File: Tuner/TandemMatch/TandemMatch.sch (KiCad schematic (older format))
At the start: 60 parts, among them J1 Conn_01x02, J10 Conn_01x01, J11 Conn_01x01, J12 Conn_01x01, J13 Conn_01x01, J14 Conn_01x01, J15 Conn_01x01, J16 Conn_01x01, J17 Conn_01x02, J18 Conn_Coaxial, J19 Conn_01x02, J2 Conn_01x02, J20 Conn_Coaxial, J21 Conn_01x01, J22 Conn_01x01, J23 Conn_01x01, J24 Conn_01x01, J25 Conn_01x01, J26 Conn_01x01, J27 Conn_01x01, J28 Conn_01x01, J29 Conn_01x01, J3 Conn_Coaxial, J30 Conn_01x01, J31 Conn_01x01, J32 Conn_01x01, J33 Conn_01x03, J34 Conn_01x01, J35 Conn_01x01, J36 Conn_01x01, J37 Conn_01x01, J38 Conn_01x01, J39 Conn_01x01, J4 Conn_Coaxial, J40 Conn_01x01, J41 Conn_01x01, J42 Conn_01x01, J5 Conn_01x01, J6 Conn_01x01, J7 Conn_01x01, J78 Conn_01x01, J79 Conn_01x01, J8 Conn_01x01, J9 Conn_01x01

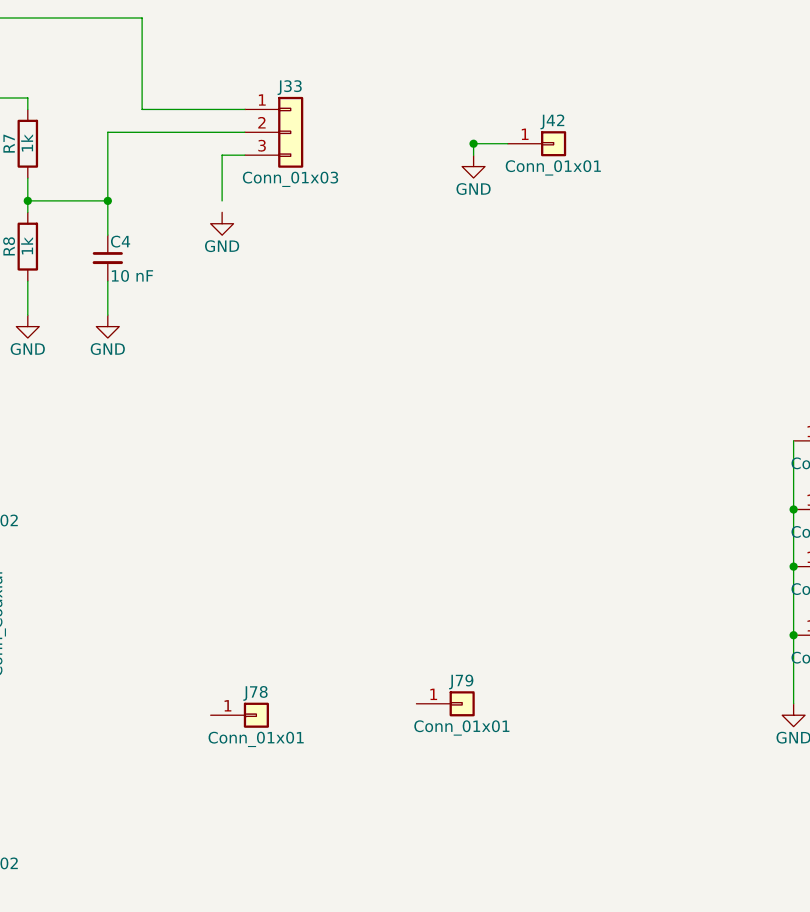
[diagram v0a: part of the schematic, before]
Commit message: Added new DelayLine board, modified TandemMatch
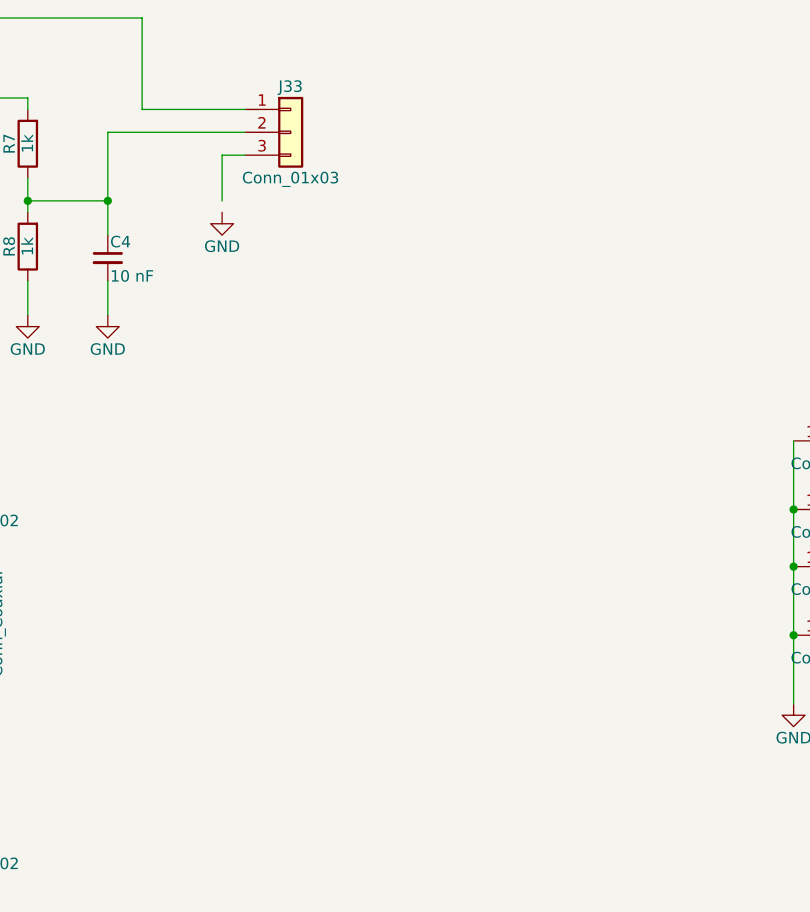
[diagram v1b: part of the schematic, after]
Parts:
- removed J42: Conn_01x01, Pin_Headers:Pin_Header_Straight_1x01_Pitch2.54mm, symbol Conn_01x01
- removed J78, J79: Conn_01x01, Connectors:1pin, symbol Conn_01x01
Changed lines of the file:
@@
 $EndComp
 $Comp
-L GND #PWR21
+L GND #PWR20
 U 1 1 5C69E6B8
 P 9450 3800
-F 0 "#PWR21" H 9450 3550 50  0001 C CNN
+F 0 "#PWR20" H 9450 3550 50  0001 C CNN
 F 1 "GND" H 9450 3650 50  0000 C CNN
 F 2 "" H 9450 3800 50  0001 C CNN
@@
 $EndComp
 $Comp
-L GND #PWR22
+L GND #PWR21
 U 1 1 5C69E7D4
 P 10250 3750
-F 0 "#PWR22" H 10250 3500 50  0001 C CNN
+F 0 "#PWR21" H 10250 3500 50  0001 C CNN
 F 1 "GND" H 10250 3600 50  0000 C CNN
 F 2 "" H 10250 3750 50  0001 C CNN
@@
 	5700 4950 5450 4950
 Connection ~ 5450 4950
-$Comp
-L Conn_01x01 J42
-U 1 1 5C6A15E5
-P 8400 1350
-F 0 "J42" H 8400 1450 50  0000 C CNN
-F 1 "Conn_01x01" H 8400 1250 50  0000 C CNN
-F 2 "Pin_Headers:Pin_Header_Straight_1x01_Pitch2.54mm" H 8400 1350 50  0001 C CNN
-F 3 "" H 8400 1350 50  0001 C CNN
-	1    8400 1350
-	1    0    0    -1
-$EndComp
-$Comp
-L GND #PWR20
-U 1 1 5C6A2A4B
-P 8050 1400
-F 0 "#PWR20" H 8050 1150 50  0001 C CNN
-F 1 "GND" H 8050 1250 50  0000 C CNN
-F 2 "" H 8050 1400 50  0001 C CNN
-F 3 "" H 8050 1400 50  0001 C CNN
-	1    8050 1400
-	1    0    0    -1
-$EndComp
-Wire Wire Line
-	8050 1350 8200 1350
-Connection ~ 8050 1350
-Wire Wire Line
-	8050 1400 8050 1350
 $Sheet
 S 9500 5450 1550 850
@@
 	5050 2550 5050 2800
 Connection ~ 5050 2800
-$Comp
-L Conn_01x01 J79
-U 1 1 5C6AED3A
-P 8000 3800
-F 0 "J79" H 8000 3900 50  0000 C CNN
-F 1 "Conn_01x01" H 8000 3700 50  0000 C CNN
-F 2 "Connectors:1pin" H 8000 3800 50  0001 C CNN
-F 3 "" H 8000 3800 50  0001 C CNN
-	1    8000 3800
-	1    0    0    -1
-$EndComp
-$Comp
-L Conn_01x01 J78
-U 1 1 5C6AED40
-P 7100 3850
-F 0 "J78" H 7100 3950 50  0000 C CNN
-F 1 "Conn_01x01" H 7100 3750 50  0000 C CNN
-F 2 "Connectors:1pin" H 7100 3850 50  0001 C CNN
-F 3 "" H 7100 3850 50  0001 C CNN
-	1    7100 3850
-	1    0    0    -1
-$EndComp
 $EndSCHEMATC

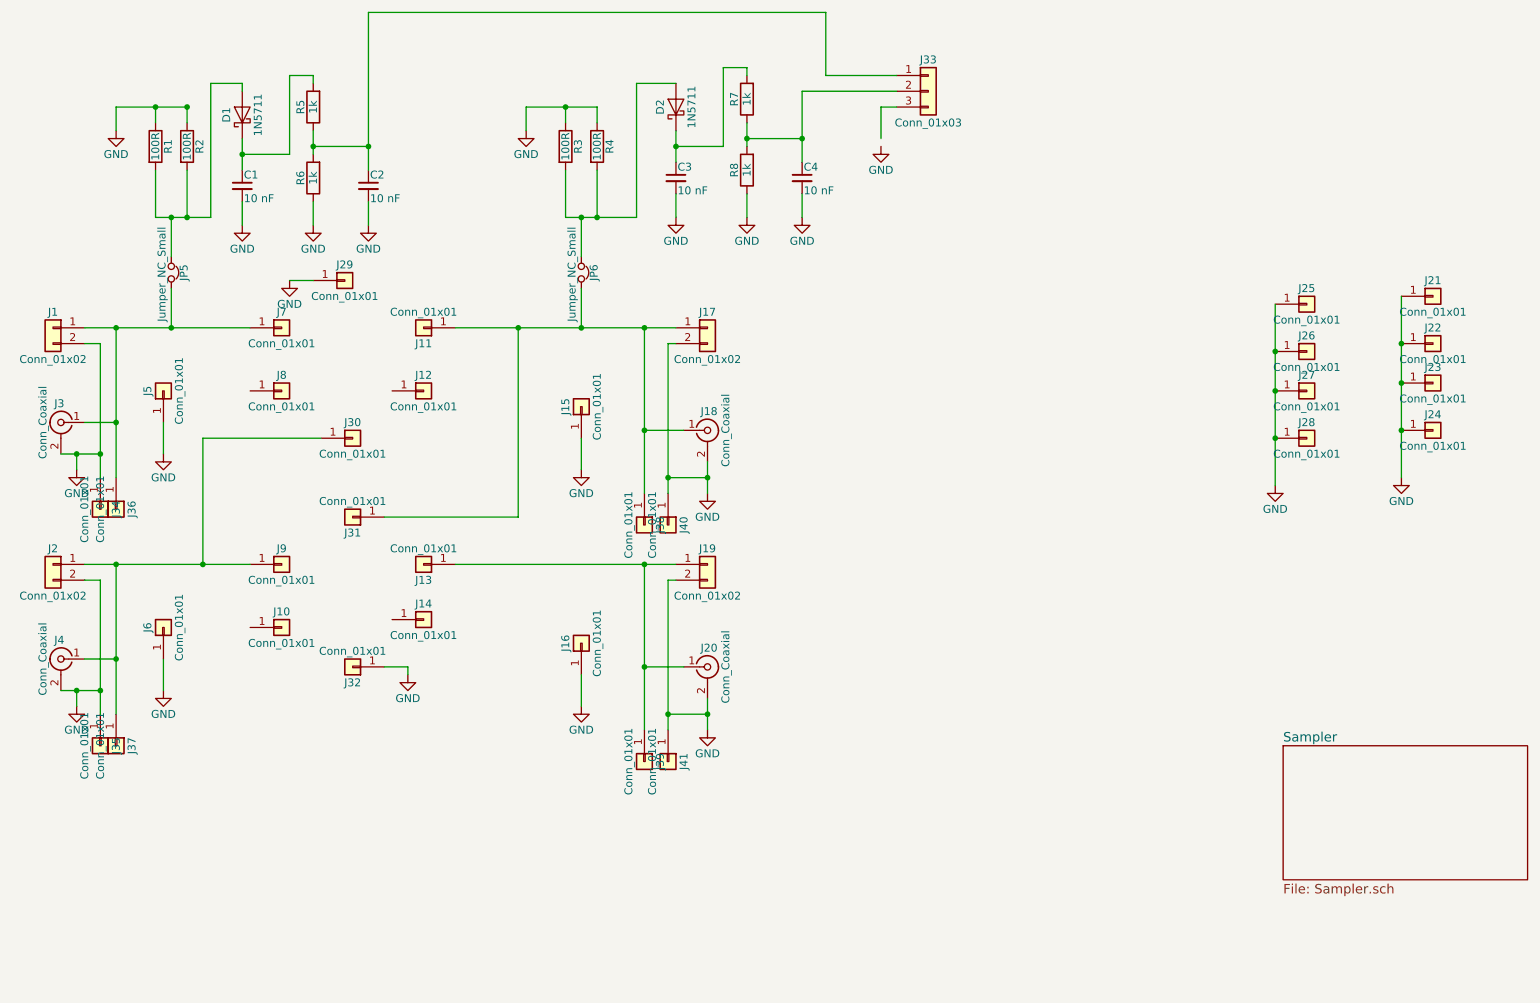
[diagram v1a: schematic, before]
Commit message: Added more instrumentation to TandemMatch, fixed grounding issue
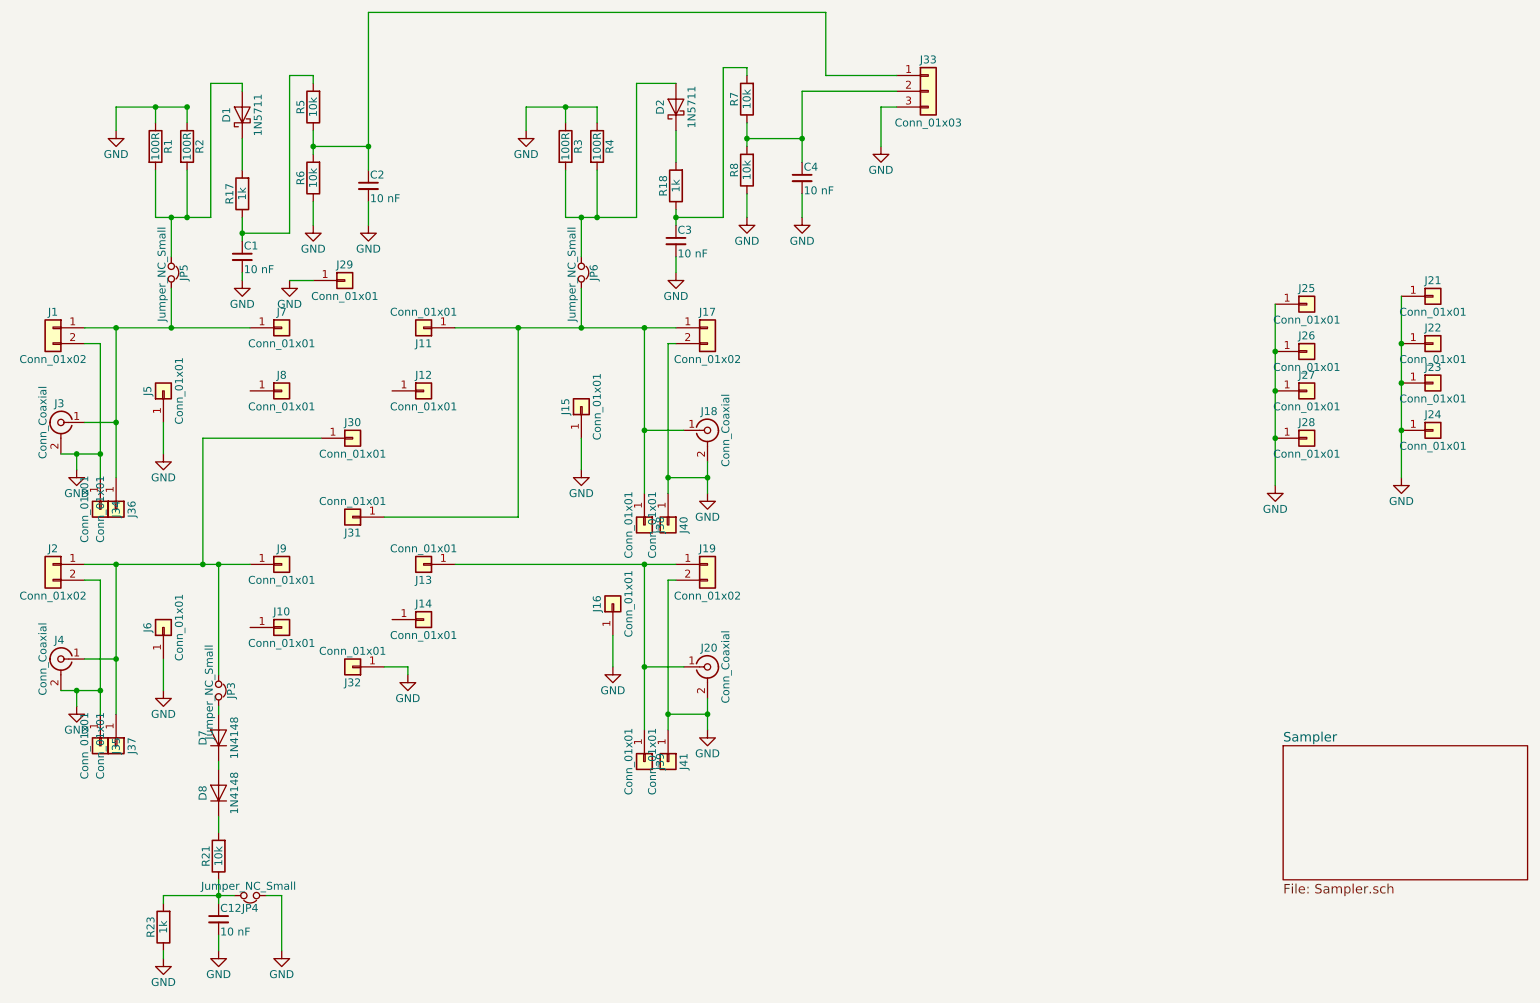
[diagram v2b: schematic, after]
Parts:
- added C12: 10 nF, Capacitors_THT:C_Disc_D5.0mm_W2.5mm_P2.50mm, symbol C_Small
- added D7, D8: 1N4148, Diodes_THT:D_DO-35_SOD27_P7.62mm_Horizontal, symbol D
- added JP3, JP4: Jumper_NC_Small, Pin_Headers:Pin_Header_Straight_1x02_Pitch2.54mm, symbol Jumper_NC_Small
- added R17, R18, R23: 1k, Resistors_THT:R_Axial_DIN0207_L6.3mm_D2.5mm_P7.62mm_Horizontal, symbol R
- added R21: 10k, Resistors_THT:R_Axial_DIN0207_L6.3mm_D2.5mm_P7.62mm_Horizontal, symbol R
- R5, R6, R7, R8: value 1k -> 10k
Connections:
- net GND: now also J33.3 (Pin_3), C12.2, JP4.1, R23.1
- net at J2.1 (Pin_1), J30.1 (Pin_1), J37.1 (Pin_1)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: now also JP3.1
- net at C1.1, R5.2: now also R17.1; no longer D1.1 (K)
- net at C3.1, R7.2: now also R18.1; no longer D2.1 (K)
- new net: D1.1 (K), R17.2
- new net: D2.1 (K), R18.2
- new net: D7.1 (K), D8.2 (A)
- new net: D7.2 (A), JP3.2
- new net: D8.1 (K), R21.2
- new net: C12.1, JP4.2, R21.1, R23.2
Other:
- moved on the sheet: C1, C3, J16

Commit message: Removed 1k resistors, did some more rearranging on TandemMatch
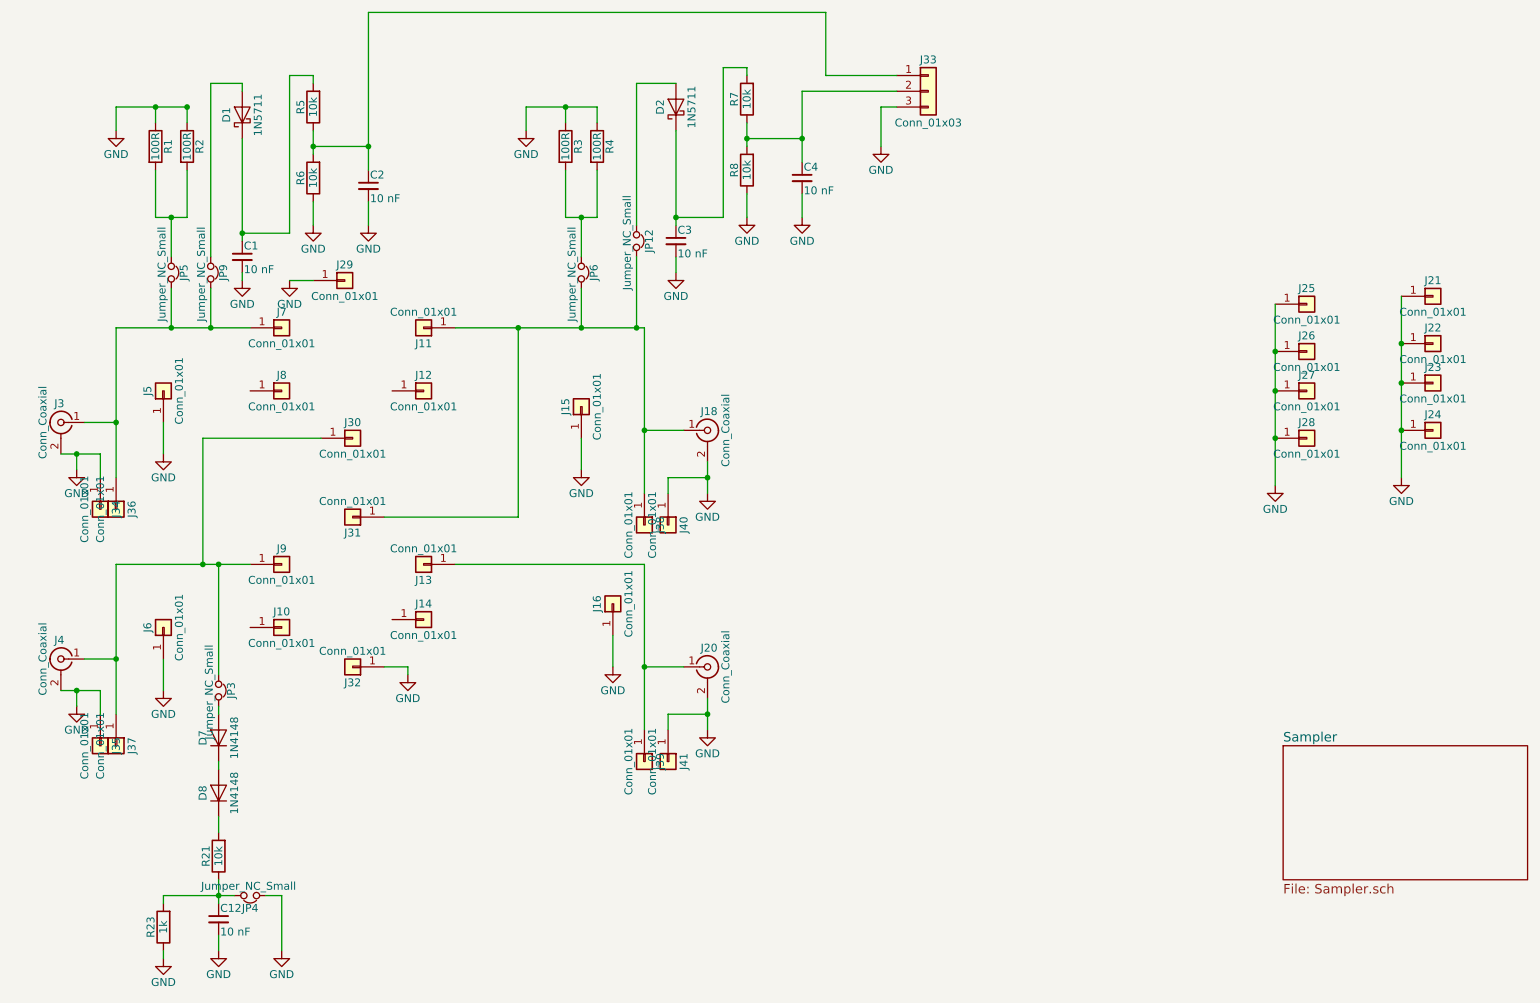
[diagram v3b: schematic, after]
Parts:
- removed J1, J17, J19, J2: Conn_01x02, Connectors_Terminal_Blocks:TerminalBlock_bornier-2_P5.08mm, symbol Conn_01x02
- removed R17, R18: 1k, Resistors_THT:R_Axial_DIN0207_L6.3mm_D2.5mm_P7.62mm_Horizontal, symbol R
- added JP12, JP9: Jumper_NC_Small, Pin_Headers:Pin_Header_Straight_1x02_Pitch2.54mm, symbol Jumper_NC_Small
- R1, R2, R3, R4: footprint Resistors_THT:R_Axial_DIN0309_L9.0mm_D3.2mm_P12.70mm_Horizontal -> TandemMatch:R_Axial_DIN0309_L9.0mm_D3.2mm_P12.70mm_Horizontal
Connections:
- net at J3.1 (In), J36.1 (Pin_1), J7.1 (Pin_1)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: now also JP9.2
- net at J11.1 (Pin_1), J18.1 (In), J31.1 (Pin_1)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: now also JP12.2
- net at JP5.1, R1.2, R2.2: no longer D1.2 (A)
- net at JP6.1, R3.2, R4.2: no longer D2.2 (A)
- net at D1.1 (K): now also C1.1, R5.2
- net at D2.1 (K): now also C3.1, R7.2
- new net: D1.2 (A), JP9.1
- new net: D2.2 (A), JP12.1

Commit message: TandenMatch now has DC-RF bias tee
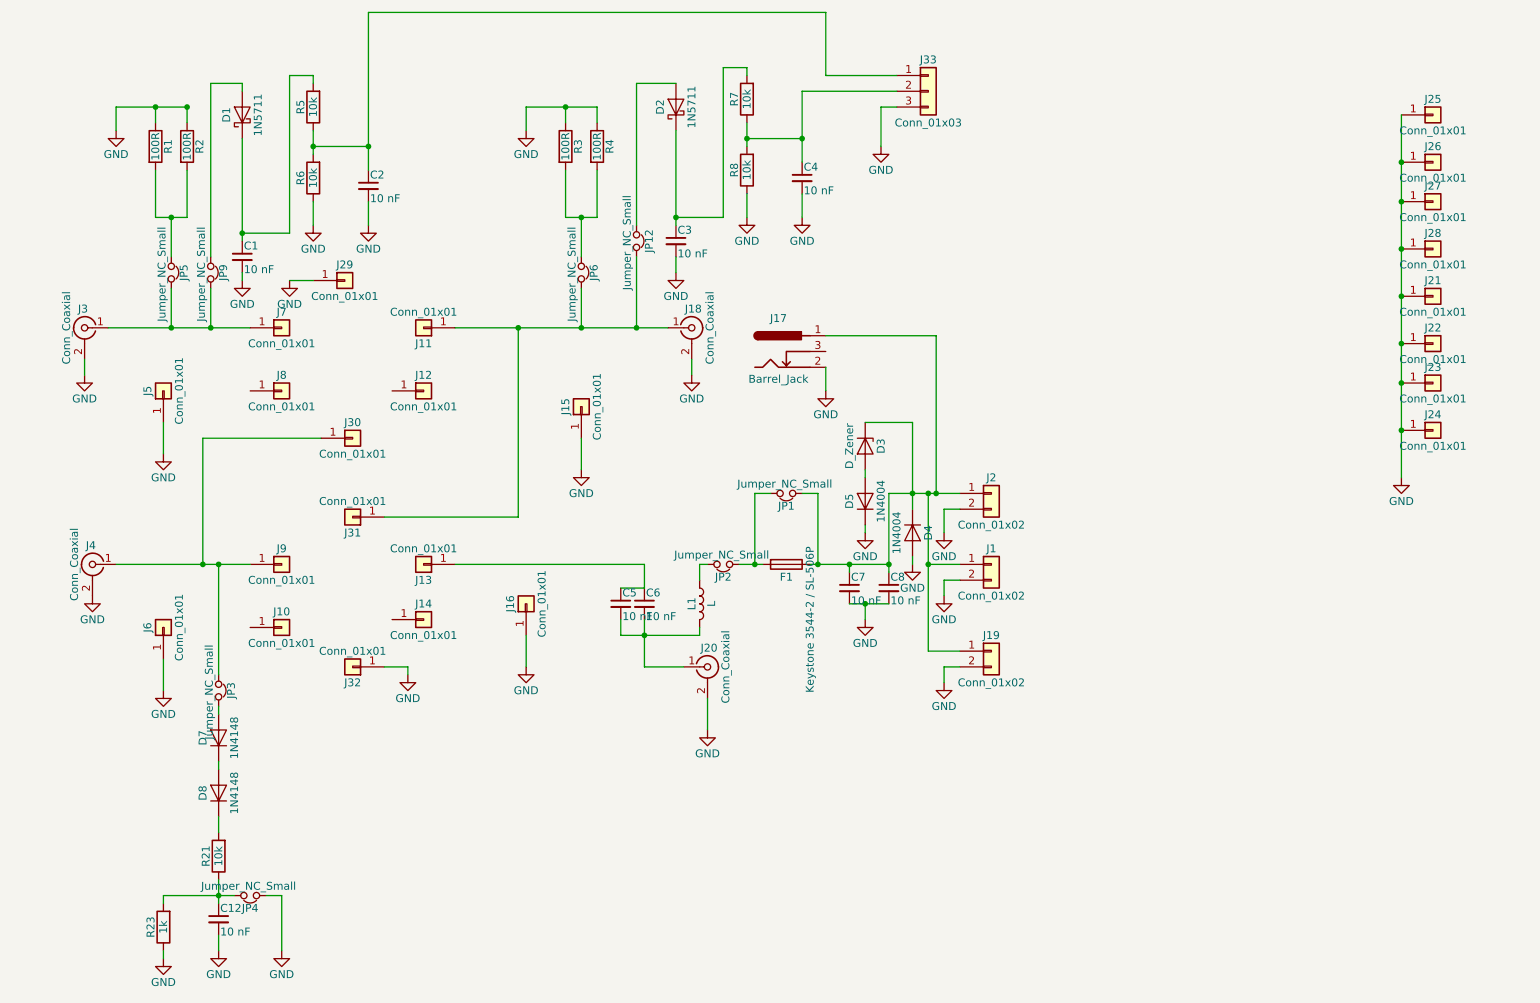
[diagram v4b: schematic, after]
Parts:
- removed J34, J35, J36, J37, J38, J39, J40, J41: Conn_01x01, Connectors:1pin, symbol Conn_01x01
- added C5, C6, C7, C8: 10 nF, Capacitors_THT:C_Disc_D5.0mm_W2.5mm_P5.00mm, symbol C_Small
- added D3: D_Zener, Diodes_THT:D_DO-41_SOD81_P10.16mm_Horizontal, symbol D_Zener
- added D4, D5: 1N4004, Diodes_THT:D_DO-41_SOD81_P10.16mm_Horizontal, symbol D
- added F1: Keystone 3544-2 / SL-506P, TandemMatch:SL506Pfuseholder, symbol Fuse
- added J1, J19, J2: Conn_01x02, Connectors_Terminal_Blocks:TerminalBlock_bornier-2_P5.08mm, symbol Conn_01x02
- added J17: Barrel_Jack, Connectors:BARREL_JACK, symbol Barrel_Jack
- added JP1, JP2: Jumper_NC_Small, Pin_Headers:Pin_Header_Straight_1x02_Pitch2.54mm, symbol Jumper_NC_Small
- added L1: L, TandemMatch:BigRFChokeInductor, symbol L
- J18, J20, J3, J4: footprint TandemMatch:bnc_90_1-1337543-0 -> TandemMatch:bnc_90_1-1337543-0_pad_combo
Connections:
- net GND: now also C7.2, C8.2, D4.2 (A), D5.1 (K), J1.2 (Pin_2), J17.2, J19.2 (Pin_2), J2.2 (Pin_2)
- net at J20.1 (In): now also C5.2, C6.2, L1.2; no longer J13.1 (Pin_1)
- new net: C5.1, C6.1, J13.1 (Pin_1)
- new net: JP2.2, L1.1
- new net: C7.1, C8.1, D3.1 (K), D4.1 (K), F1.1, J1.1 (Pin_1), J17.1, J19.1 (Pin_1), J2.1 (Pin_1), JP1.1
- new net: F1.2, JP1.2, JP2.1
- new net: D3.2 (A), D5.2 (A)
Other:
- moved on the sheet: J16, J18, J3, J4
